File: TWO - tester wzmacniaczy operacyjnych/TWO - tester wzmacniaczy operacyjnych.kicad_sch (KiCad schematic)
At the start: 0 parts

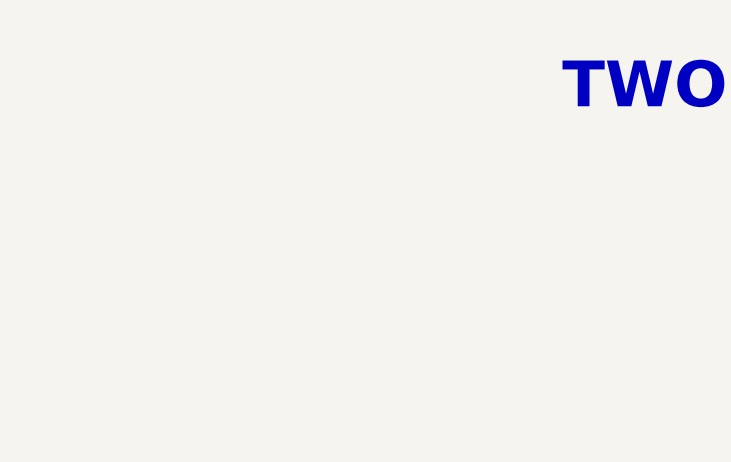
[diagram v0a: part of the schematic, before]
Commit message: Added Used Components and Basic project requirements
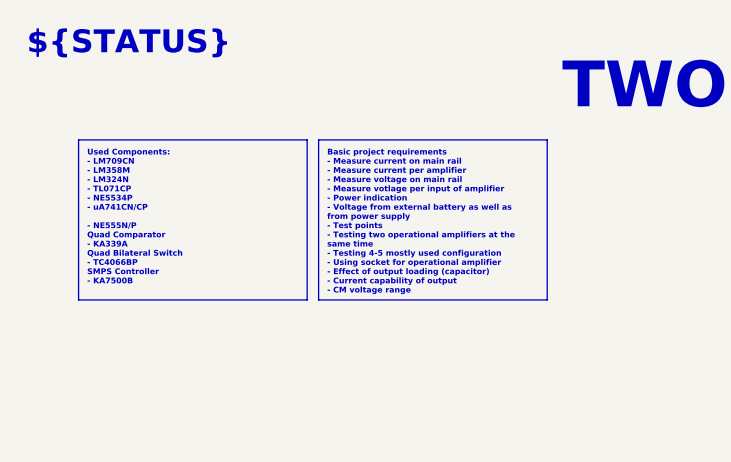
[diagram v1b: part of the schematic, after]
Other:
- note added: "${STATUS}"
- company: (none) -> ${COMPANY}
- title: (none) -> ${TITLE}
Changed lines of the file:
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@@
 	(generator_version "9.0")
 	(paper "A4")
+	(title_block
+		(title "${TITLE}")
+		(date "2025-03-28")
+		(rev "${REVISION}")
+		(company "${COMPANY}")
+	)
 	(polyline
 		(pts
@@
 		)
 	)
+	(text "${STATUS}"
+		(exclude_from_sim no)
+		(at 18.288 14.732 0)
+		(effects
+			(font
+				(size 2.54 2.54)
+				(thickness 0.508)
+				(bold yes)
+				(color 255 0 143 1)
+			)
+		)
+	)
+	(text_box "Basic project requirements\n- Measure current on main rail\n- Measure current per amplifier\n- Measure voltage on main rail\n- Measure votlage per input of amplifier\n- Power indication\n- Voltage from external battery as well as from power supply\n- Test points\n- Testing two operational amplifiers at the same time\n- Testing 4-5 mostly used configuration\n- Using socket for operational amplifier\n- Effect of output loading (capacitor)\n- Current capability of output\n- CM voltage range"
+		(exclude_from_sim no)
+		(at 39.37 25.4 0)
+		(size 25.4 17.78)
+		(margins 0.9525 0.9525 0.9525 0.9525)
+		(stroke
+			(width 0)
+			(type solid)
+		)
+		(fill
+			(type color)
+			(color 255 255 194 1)
+		)
+		(effects
+			(font
+				(size 0.635 0.635)
+				(thickness 0.508)
+				(bold yes)
+			)
+			(justify left top)
+		)
+	)
+	(text_box "Used Components:\n- LM709CN\n- LM358M\n- LM324N\n- TL071CP\n- NE5534P\n- uA741CN/CP\n\n- NE555N/P\nQuad Comparator\n- KA339A\nQuad Bilateral Switch\n- TC4066BP\nSMPS Controller\n- KA7500B"
+		(exclude_from_sim no)
+		(at 12.7 25.4 0)
+		(size 25.4 17.78)
+		(margins 0.9525 0.9525 0.9525 0.9525)
+		(stroke
+			(width 0)
+			(type solid)
+		)
+		(fill
+			(type color)
+			(color 255 255 194 1)
+		)
+		(effects
+			(font
+				(size 0.635 0.635)
+				(thickness 0.508)
+				(bold yes)
+			)
+			(justify left top)
+		)
+	)
